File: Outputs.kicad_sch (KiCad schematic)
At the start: 0 parts

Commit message: update
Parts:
- added M1: Motor_Servo, Connector_PinHeader_2.54mm:PinHeader_1x03_P2.54mm_Vertical, symbol Motor:Motor_Servo
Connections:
- new net +3.3V: M1.2 (+)
- new net GND: M1.3 (-)
- new net PWM_0: M1.1 (PWM)

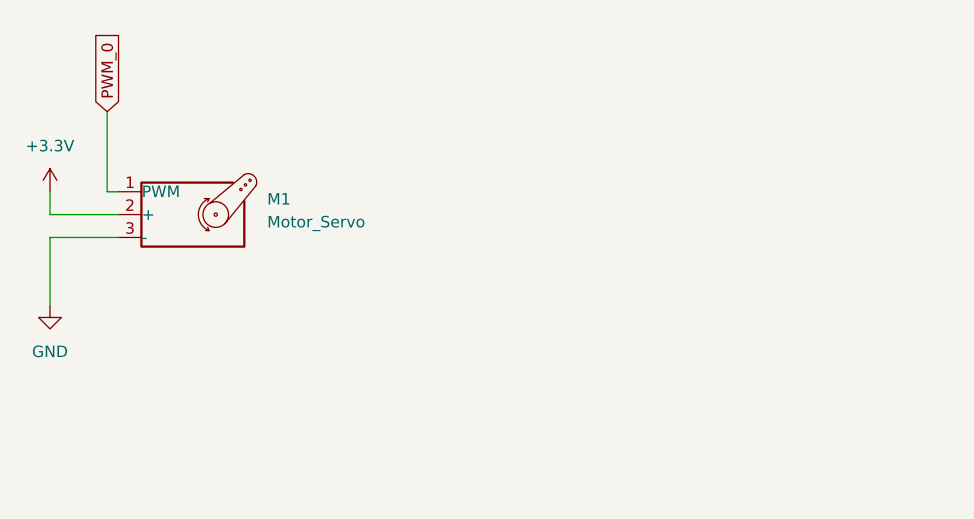
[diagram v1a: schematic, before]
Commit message: Added output headers
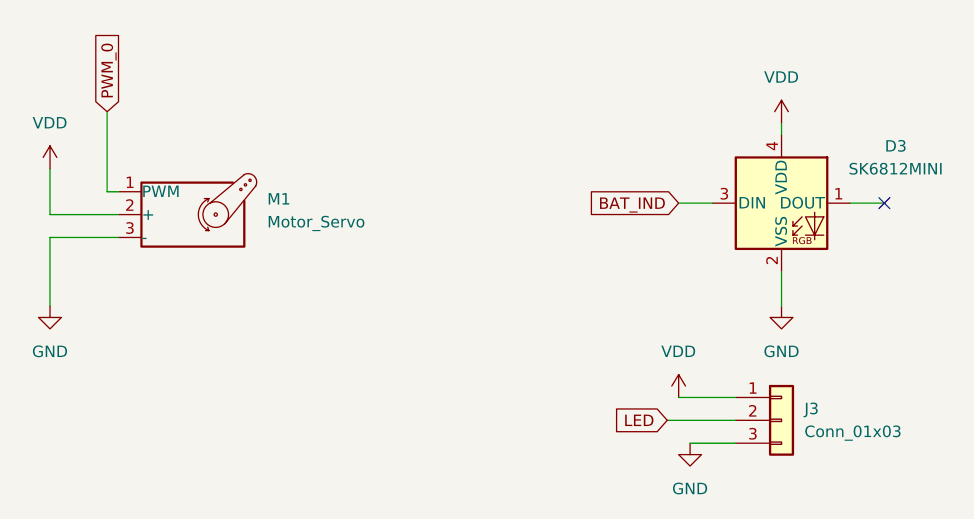
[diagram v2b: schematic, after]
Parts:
- added D3: SK6812MINI, LED_SMD:LED_SK6812MINI_PLCC4_3.5x3.5mm_P1.75mm, symbol LED:SK6812MINI
- added J3: Conn_01x03, Connector_PinHeader_2.54mm:PinHeader_1x03_P2.54mm_Horizontal, symbol Connector_Generic:Conn_01x03
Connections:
- net GND: now also D3.2 (VSS), J3.3 (Pin_3)
- net +3.3V renamed VDD
- net VDD: now also D3.4 (VDD), J3.1 (Pin_1)
- new net BAT_IND: D3.3 (DIN)
- new net LED: J3.2 (Pin_2)
- no-connect marks 0 -> 1

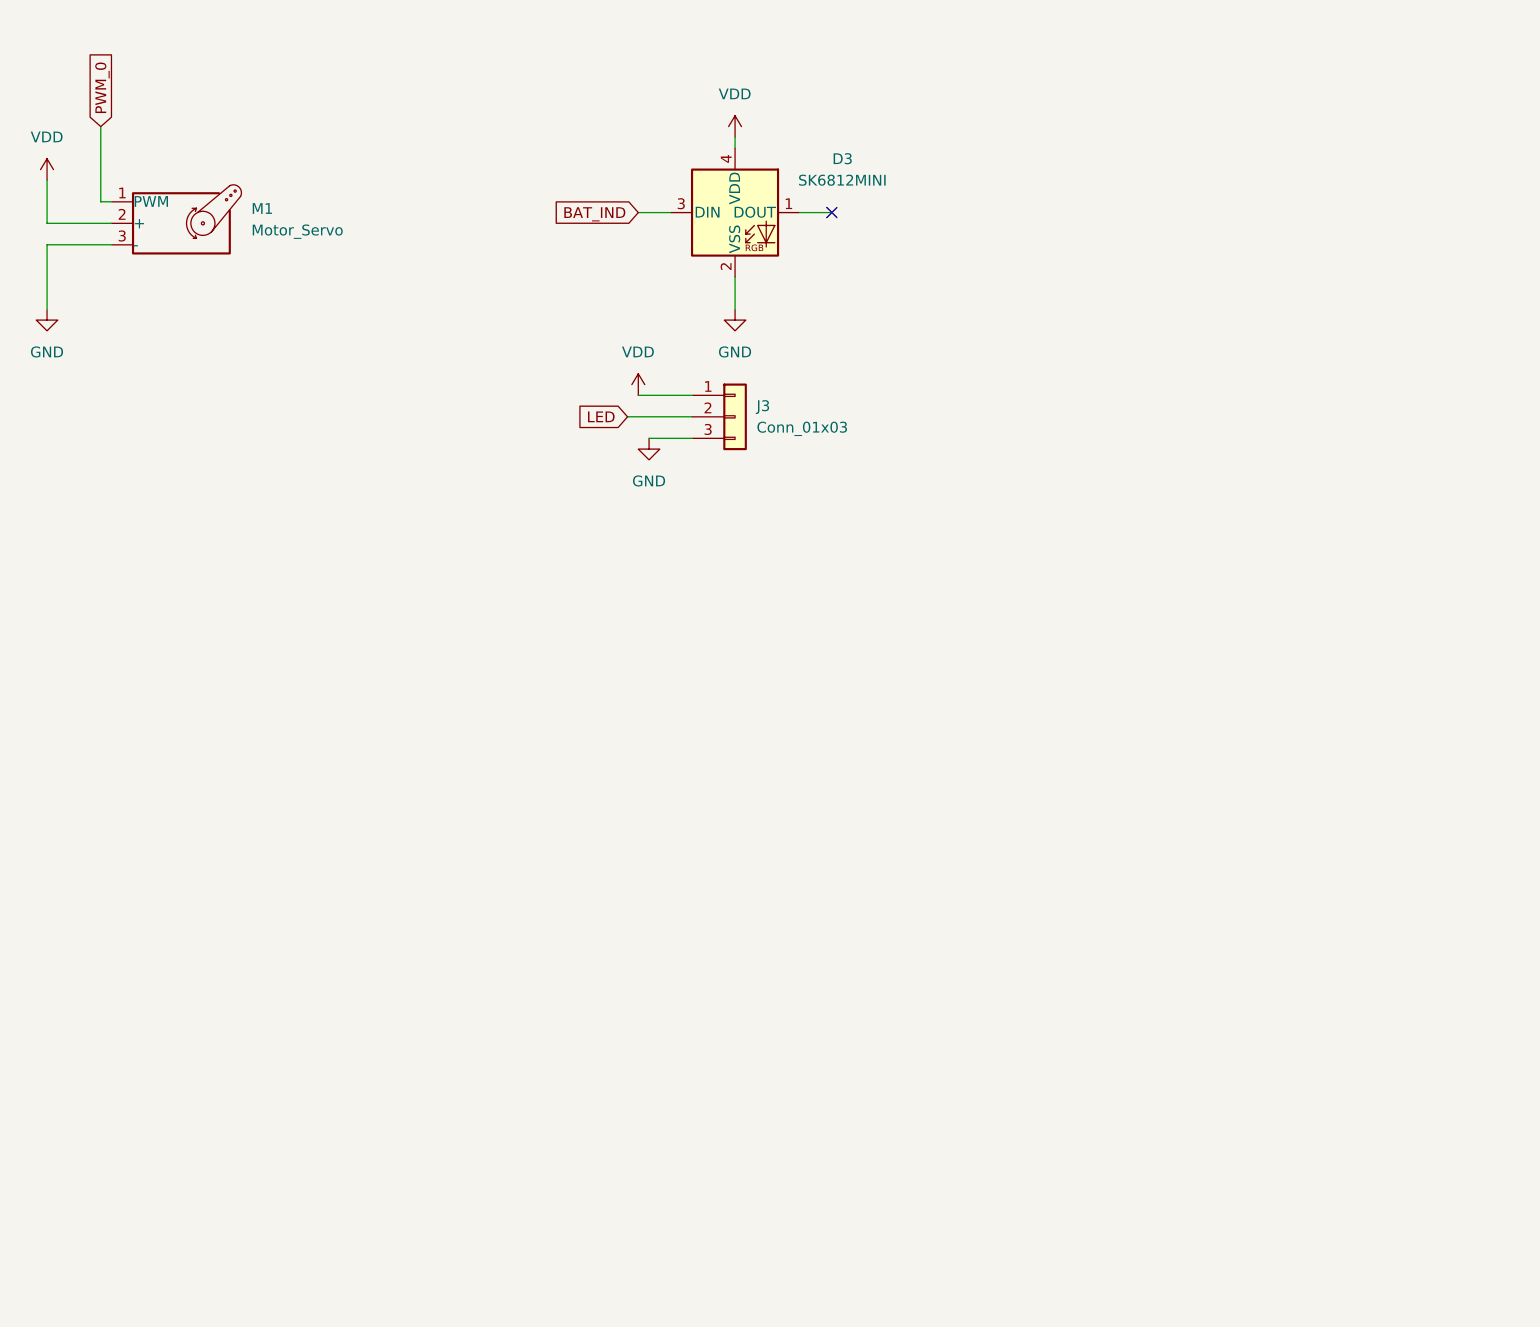
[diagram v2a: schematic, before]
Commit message: Added microphone, fuse
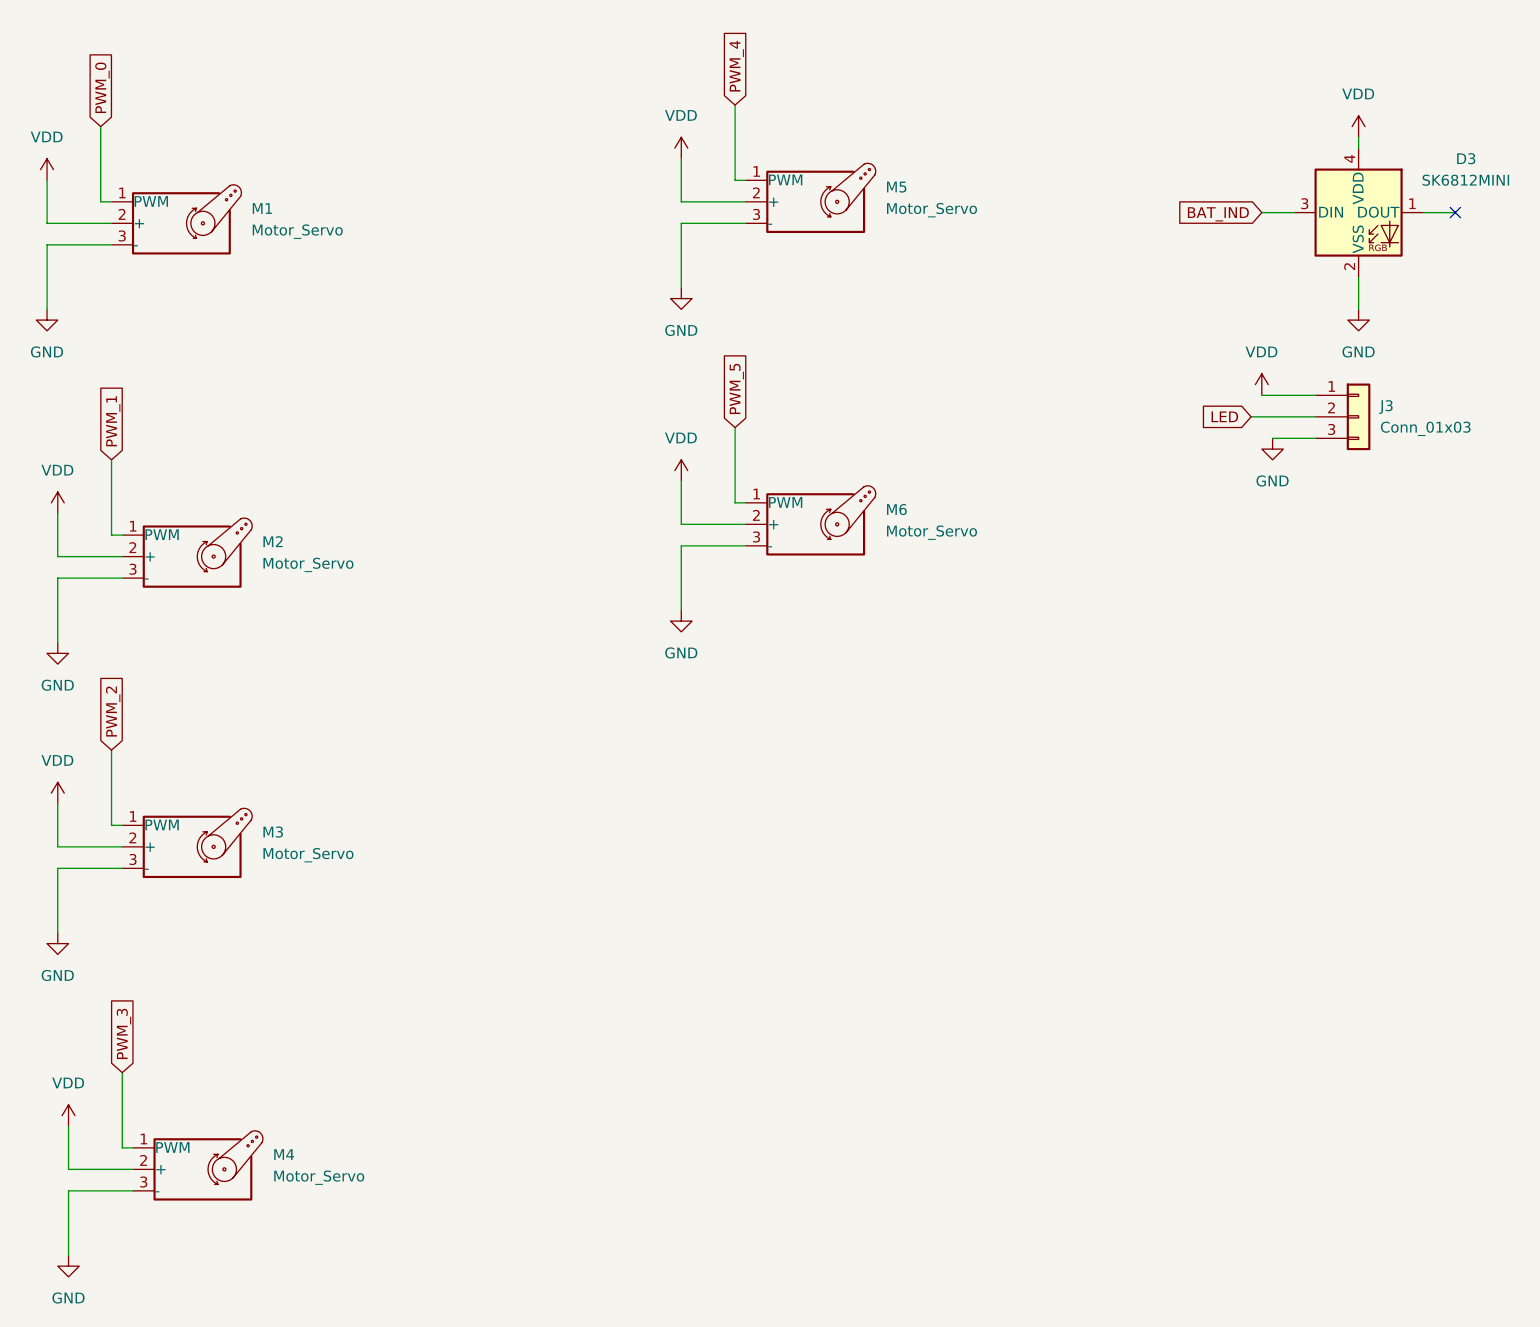
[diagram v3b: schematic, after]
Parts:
- added M2, M3, M4, M5, M6: Motor_Servo, Connector_PinHeader_2.54mm:PinHeader_1x03_P2.54mm_Vertical, symbol Motor:Motor_Servo
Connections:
- net GND: now also M2.3 (-), M3.3 (-), M4.3 (-), M5.3 (-), M6.3 (-)
- net VDD: now also M2.2 (+), M3.2 (+), M4.2 (+), M5.2 (+), M6.2 (+)
- new net PWM_1: M2.1 (PWM)
- new net PWM_2: M3.1 (PWM)
- new net PWM_3: M4.1 (PWM)
- new net PWM_4: M5.1 (PWM)
- new net PWM_5: M6.1 (PWM)
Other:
- moved on the sheet: D3, J3

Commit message: PCB layout
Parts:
- added C24: .1u, Capacitor_SMD:C_0603_1608Metric, symbol Device:C
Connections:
- net GND: now also C24.1
- net VDD: now also C24.2
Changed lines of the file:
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@@
 	(generator_version "8.0")
 	(paper "A4")
+	(junction
+		(at 212.09 29.21)
+		(diameter 0)
+		(color 0 0 0 0)
+	)
 	(no_connect
 		(at 223.52 41.91)
@@
 	(wire
 		(pts
+			(xy 212.09 29.21) (xy 212.09 34.29)
+		)
+		(stroke
+			(width 0)
+			(type default)
+		)
+	)
+	(wire
+		(pts
 			(xy 58.42 119.38) (xy 66.04 119.38)
 		)
@@
 	(wire
 		(pts
-			(xy 212.09 33.02) (xy 212.09 34.29)
+			(xy 212.09 25.4) (xy 212.09 29.21)
 		)
 		(stroke
@@
 	(wire
 		(pts
+			(xy 208.28 29.21) (xy 212.09 29.21)
+		)
+		(stroke
+			(width 0)
+			(type default)
+		)
+	)
+	(wire
+		(pts
 			(xy 132.08 81.28) (xy 139.7 81.28)
 		)
@@
 		(pts
 			(xy 138.43 29.21) (xy 138.43 38.1)
+		)
+		(stroke
+			(width 0)
+			(type default)
+		)
+	)
+	(wire
+		(pts
+			(xy 200.66 34.29) (xy 200.66 29.21)
 		)
 		(stroke
@@
 	)
 	(symbol
+		(lib_id "power:VDD")
+		(at 212.09 25.4 0)
+		(unit 1)
+		(exclude_from_sim no)
+		(in_bom yes)
+		(on_board yes)
+		(dnp no)
+		(fields_autoplaced yes)
+		(property "Reference" "#PWR030"
+			(at 212.09 29.21 0)
+			(effects
+				(font
+					(size 1.27 1.27)
+				)
+				(hide yes)
+			)
+		)
+		(property "Value" "VDD"
+			(at 212.09 20.32 0)
+			(effects
+				(font
+					(size 1.27 1.27)
+				)
+			)
+		)
+		(property "Footprint" ""
+			(at 212.09 25.4 0)
+			(effects
+				(font
+					(size 1.27 1.27)
+				)
+				(hide yes)
+			)
+		)
+		(property "Datasheet" ""
+			(at 212.09 25.4 0)
+			(effects
+				(font
+					(size 1.27 1.27)
+				)
+				(hide yes)
+			)
+		)
+		(property "Description" "Power symbol creates a global label with name \"VDD\""
+			(at 212.09 25.4 0)
+			(effects
+				(font
+					(size 1.27 1.27)
+				)
+				(hide yes)
+			)
+		)
+		(pin "1"
+		)
+		(instances
+			(project "nrfMain"
+				(path "/4b478080-1b18-4cae-a6eb-51454cf43595/60577678-b461-48ab-a77f-5a5fa4853d50"
+					(reference "#PWR030")
+					(unit 1)
+				)
+			)
+		)
+	)
+	(symbol
 		(lib_id "Connector_Generic:Conn_01x03")
 		(at 212.09 66.04 0)
@@
 	)
 	(symbol
-		(lib_id "power:VDD")
-		(at 212.09 33.02 0)
-		(unit 1)
-		(exclude_from_sim no)
-		(in_bom yes)
-		(on_board yes)
-		(dnp no)
-		(fields_autoplaced yes)
-		(property "Reference" "#PWR030"
-			(at 212.09 36.83 0)
-			(effects
-				(font
-					(size 1.27 1.27)
-				)
-				(hide yes)
-			)
-		)
-		(property "Value" "VDD"
-			(at 212.09 27.94 0)
+		(lib_id "power:GND")
+		(at 200.66 34.29 0)
+		(unit 1)
+		(exclude_from_sim no)
+		(in_bom yes)
+		(on_board yes)
+		(dnp no)
+		(fields_autoplaced yes)
+		(property "Reference" "#PWR079"
+			(at 200.66 40.64 0)
+			(effects
+				(font
+					(size 1.27 1.27)
+				)
+				(hide yes)
+			)
+		)
+		(property "Value" "GND"
+			(at 200.66 39.37 0)
 			(effects
 				(font
@@
 		)
 		(property "Footprint" ""
-			(at 212.09 33.02 0)
+			(at 200.66 34.29 0)
 			(effects
 				(font
@@
 		)
 		(property "Datasheet" ""
-			(at 212.09 33.02 0)
-			(effects
-				(font
-					(size 1.27 1.27)
-				)
-				(hide yes)
-			)
-		)
-		(property "Description" "Power symbol creates a global label with name \"VDD\""
-			(at 212.09 33.02 0)
+			(at 200.66 34.29 0)
+			(effects
+				(font
+					(size 1.27 1.27)
+				)
+				(hide yes)
+			)
+		)
+		(property "Description" "Power symbol creates a global label with name \"GND\" , ground"
+			(at 200.66 34.29 0)
 			(effects
 				(font
@@
 			(project "nrfMain"
 				(path "/4b478080-1b18-4cae-a6eb-51454cf43595/60577678-b461-48ab-a77f-5a5fa4853d50"
-					(reference "#PWR030")
+					(reference "#PWR079")
 					(unit 1)
 				)
@@
 					(unit 1)
 				)
+			)
+		)
+	)
+	(symbol
+		(lib_id "Device:C")
+		(at 204.47 29.21 90)
+		(unit 1)
+		(exclude_from_sim no)
+		(in_bom yes)
+		(on_board yes)
+		(dnp no)
+		(fields_autoplaced yes)
+		(property "Reference" "C24"
+			(at 204.47 21.59 90)
+			(effects
+				(font
+					(size 1.27 1.27)
+				)
+			)
+		)
+		(property "Value" ".1u"
+			(at 204.47 24.13 90)
+			(effects
+				(font
+					(size 1.27 1.27)
+				)
+			)
+		)
+		(property "Footprint" "Capacitor_SMD:C_0603_1608Metric"
+			(at 208.28 28.2448 0)
+			(effects
+				(font
+					(size 1.27 1.27)
+				)
+				(hide yes)
+			)
+		)
+		(property "Datasheet" "~"
+			(at 204.47 29.21 0)
+			(effects
+				(font
+					(size 1.27 1.27)
+				)
+				(hide yes)
+			)
+		)
+		(property "Description" "Unpolarized capacitor"
+			(at 204.47 29.21 0)
+			(effects
+				(font
+					(size 1.27 1.27)
+				)
+				(hide yes)
+			)
+		)
+		(property "LCSC PN" "C14663"
+			(at 204.47 29.21 0)
+			(effects
+				(font
+					(size 1.27 1.27)
+				)
+				(hide yes)
+			)
+		)
+		(pin "2"
+		)
+		(pin "1"
+		)
+		(instances
+			(project "nrfMain"
+				(path "/4b478080-1b18-4cae-a6eb-51454cf43595/60577678-b461-48ab-a77f-5a5fa4853d50"
+					(reference "C24")
+					(unit 1)
+				)

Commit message: Made modifications from fabrication
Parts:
- C24: MPN (none) -> C14663
- D3: MPN (none) -> C2922787
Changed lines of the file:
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@@
+			)
+		)
+		(property "MPN" "C2922787"
+			(at 212.09 41.91 0)
+			(effects
+				(font
+					(size 1.27 1.27)
+				)
+				(hide yes)
 			)
 		)
@@
 			(effects
 				(font
+					(size 1.27 1.27)
+				)
+				(hide yes)
+			)
+		)
+		(property "MPN" "C14663"
+			(at 204.47 29.21 90)
+			(effects
+				(font
